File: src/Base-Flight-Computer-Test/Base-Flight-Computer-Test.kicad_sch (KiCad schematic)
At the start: 58 parts, among them J1 Jumper_NO, P1 1984659, P2 USB, P3 0530470610, P4 1984659, P5 B2B-PH-K-SLFSN_JST, Q1 QS5U17TR, Q2 2N7002W-7-F, Q3 2N7002W-7-F, Q4 QS5U17TR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

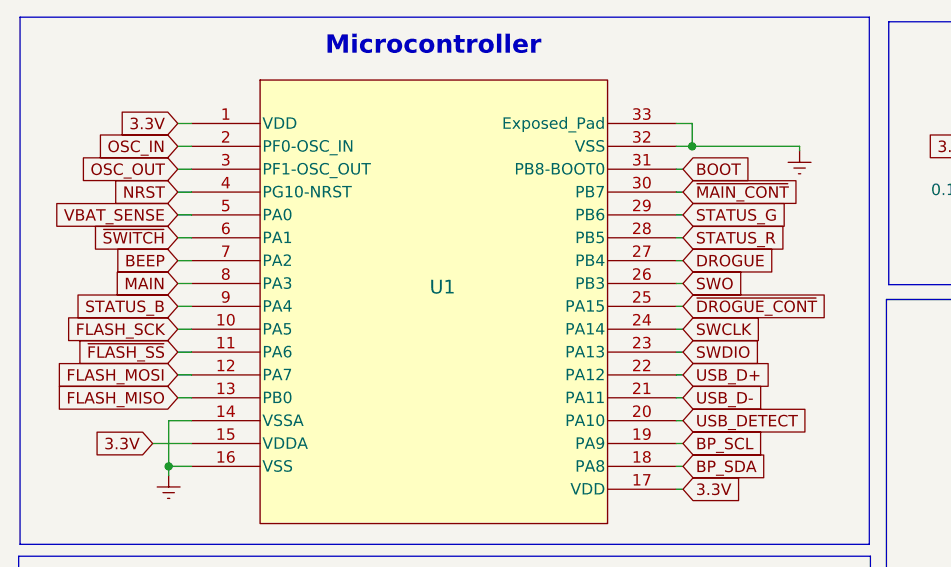
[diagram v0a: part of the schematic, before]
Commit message: completed initial test layout
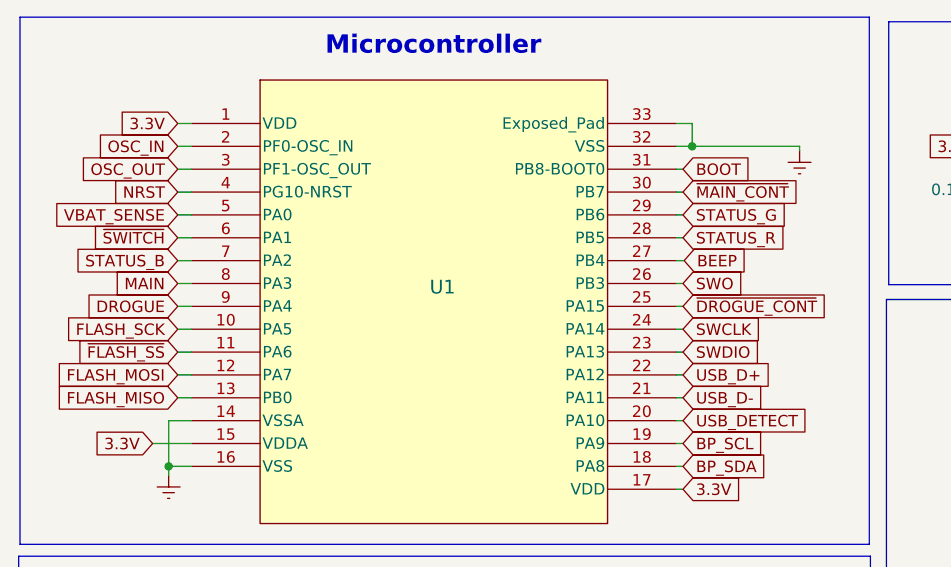
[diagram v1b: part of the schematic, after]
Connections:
- net BEEP: now also U1.27 (PB4); no longer U1.7 (PA2)
- net DROGUE: now also U1.9 (PA4); no longer U1.27 (PB4)
- net STATUS_B: now also U1.7 (PA2); no longer U1.9 (PA4)

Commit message: plotted schematic
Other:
- company: Sun Devil Rocketry Avionics -> Author: Colton Acosta
- title: Flight Computer Lite -> Base Flight Computer  - Test
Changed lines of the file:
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@@
   (paper "A4")
   (title_block
-    (title "Flight Computer Lite")
-    (date "2022-12-17")
+    (title "Base Flight Computer  - Test")
+    (date "2023-05-27")
     (rev "1.0")
-    (company "Sun Devil Rocketry Avionics")
-    (comment 1 "Author: Colton Acosta")
+    (company "Author: Colton Acosta")
   )
   (junction (at 144.399 174.117) (diameter 0) (color 0 0 0 0)
